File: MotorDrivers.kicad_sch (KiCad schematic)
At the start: 0 parts

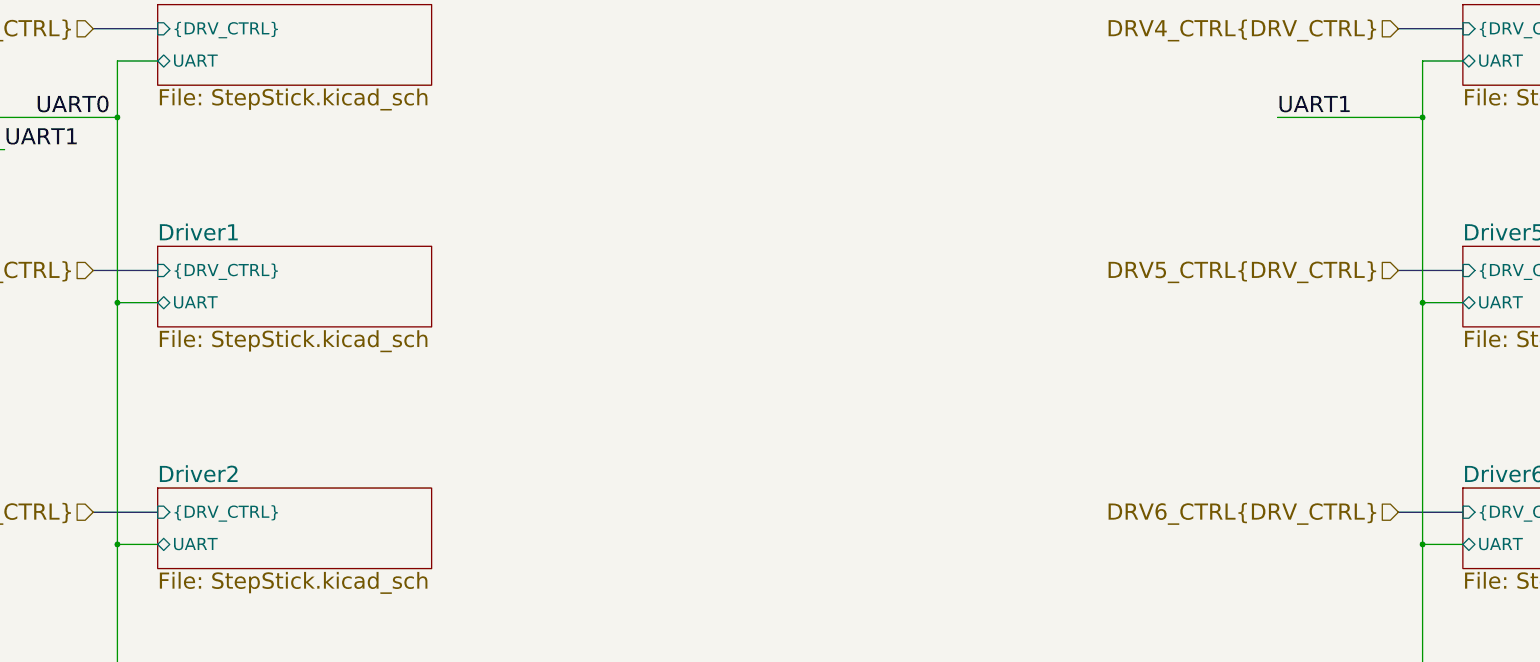
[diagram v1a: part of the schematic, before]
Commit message: Attach ethernet to PL, layout and route
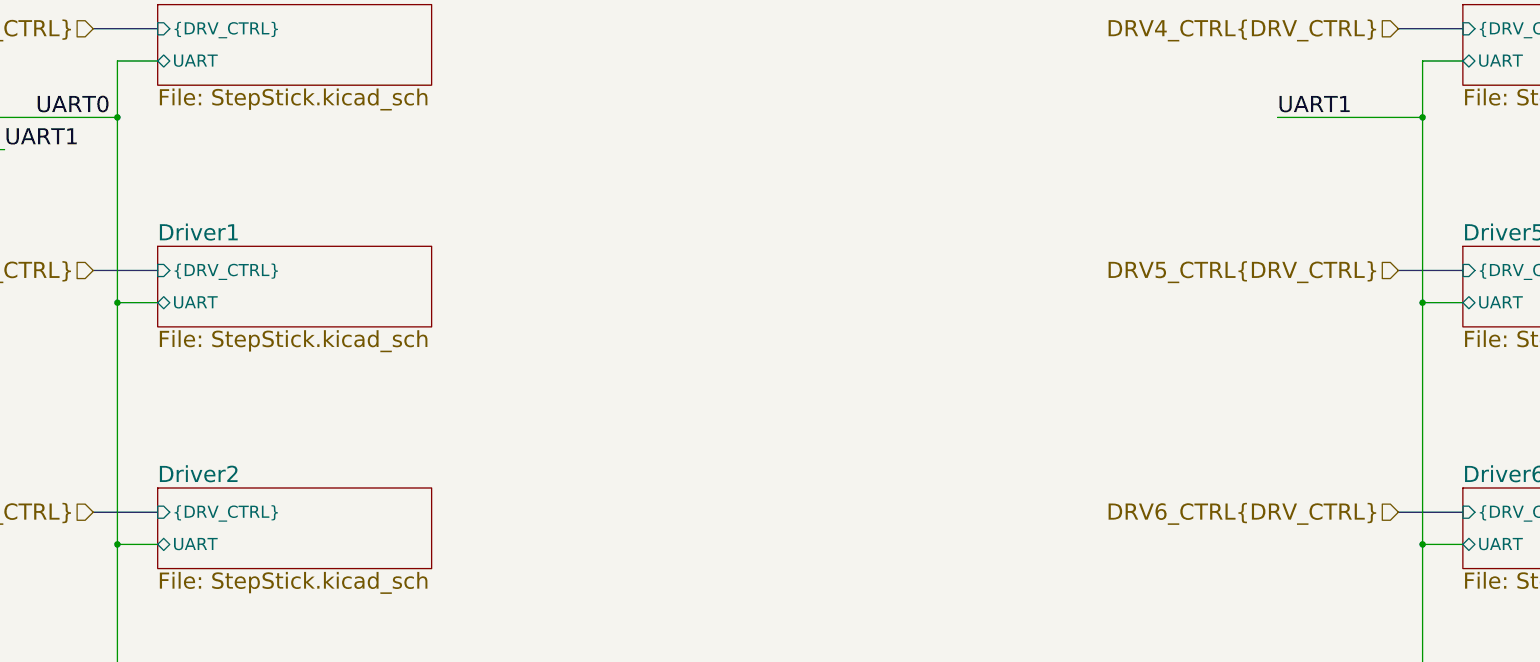
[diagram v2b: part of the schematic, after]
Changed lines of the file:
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@@
-(kicad_sch (version 20200714) (host eeschema "5.99.0-unknown-bf445c1~102~ubuntu20.04.1")
-  (page 1 15)
+(kicad_sch (version 20200714) (host eeschema "5.99.0-unknown-a146cd9~102~ubuntu20.04.1")
+  (page 7 15)
   (paper "B")
   (title_block
@@
     (comment 1 "Drawn by: Cameron McQuinn")
   )
-  (junction (at 85.09 78.74) (diameter 0) (color 0 0 0 0))
-  (junction (at 85.09 107.95) (diameter 0) (color 0 0 0 0))
-  (junction (at 85.09 146.05) (diameter 0) (color 0 0 0 0))
-  (junction (at 290.83 78.74) (diameter 0) (color 0 0 0 0))
-  (junction (at 290.83 107.95) (diameter 0) (color 0 0 0 0))
-  (junction (at 290.83 146.05) (diameter 0) (color 0 0 0 0))
+  (junction (at 85.09 78.74) (diameter 1.016) (color 0 0 0 0))
+  (junction (at 85.09 107.95) (diameter 1.016) (color 0 0 0 0))
+  (junction (at 85.09 146.05) (diameter 1.016) (color 0 0 0 0))
+  (junction (at 290.83 78.74) (diameter 1.016) (color 0 0 0 0))
+  (junction (at 290.83 107.95) (diameter 1.016) (color 0 0 0 0))
+  (junction (at 290.83 146.05) (diameter 1.016) (color 0 0 0 0))
   (bus_entry (at 59.69 81.28) (size 2.54 -2.54)
     (stroke (width 0.1524) (type solid) (color 0 0 0 0))

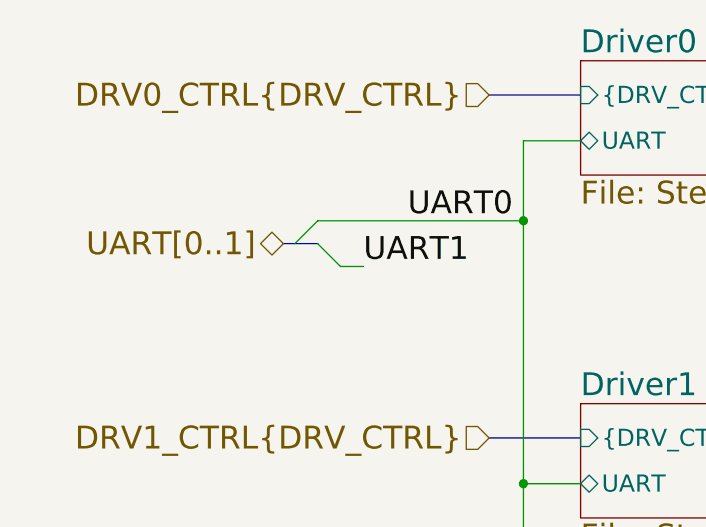
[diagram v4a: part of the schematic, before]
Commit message: Move Ethernet PHY to left side of board
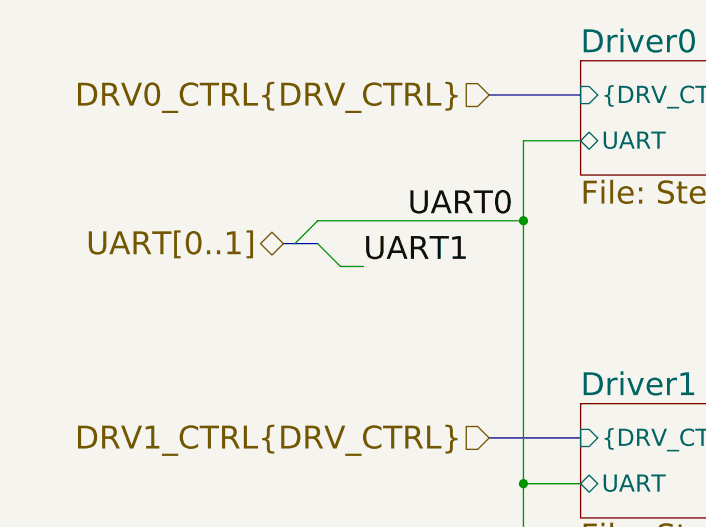
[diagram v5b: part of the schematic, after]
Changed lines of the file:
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@@
-(kicad_sch (version 20200714) (host eeschema "5.99.0-unknown-829316fad~102~ubuntu20.04.1")
+(kicad_sch (version 20200828) (generator eeschema)
   (page 7 15)
   (paper "B")
@@
     (stroke (width 0) (type solid) (color 0 0 0 0))
   )
-  (bus (pts (xy 58.42 81.28) (xy 62.23 81.28))
+  (bus (pts (xy 58.42 81.28) (xy 59.69 81.28))
     (stroke (width 0) (type solid) (color 0 0 0 0))
   )
+  (bus (pts (xy 59.69 81.28) (xy 62.23 81.28))
+    (stroke (width 0) (type solid) (color 0 0 0 0))
+  )
